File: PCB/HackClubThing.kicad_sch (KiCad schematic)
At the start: 13 parts, among them SW1 SW_Push, SW2 SW_Push, SW3 SW_Push, SW4 SW_Push, SW5 SW_Push, SW6 RotaryEncoder_Switch, U1 MOUDLE-SEEEDUINO-XIAO, U2 ER_OLEDM0.91_1x-I2C

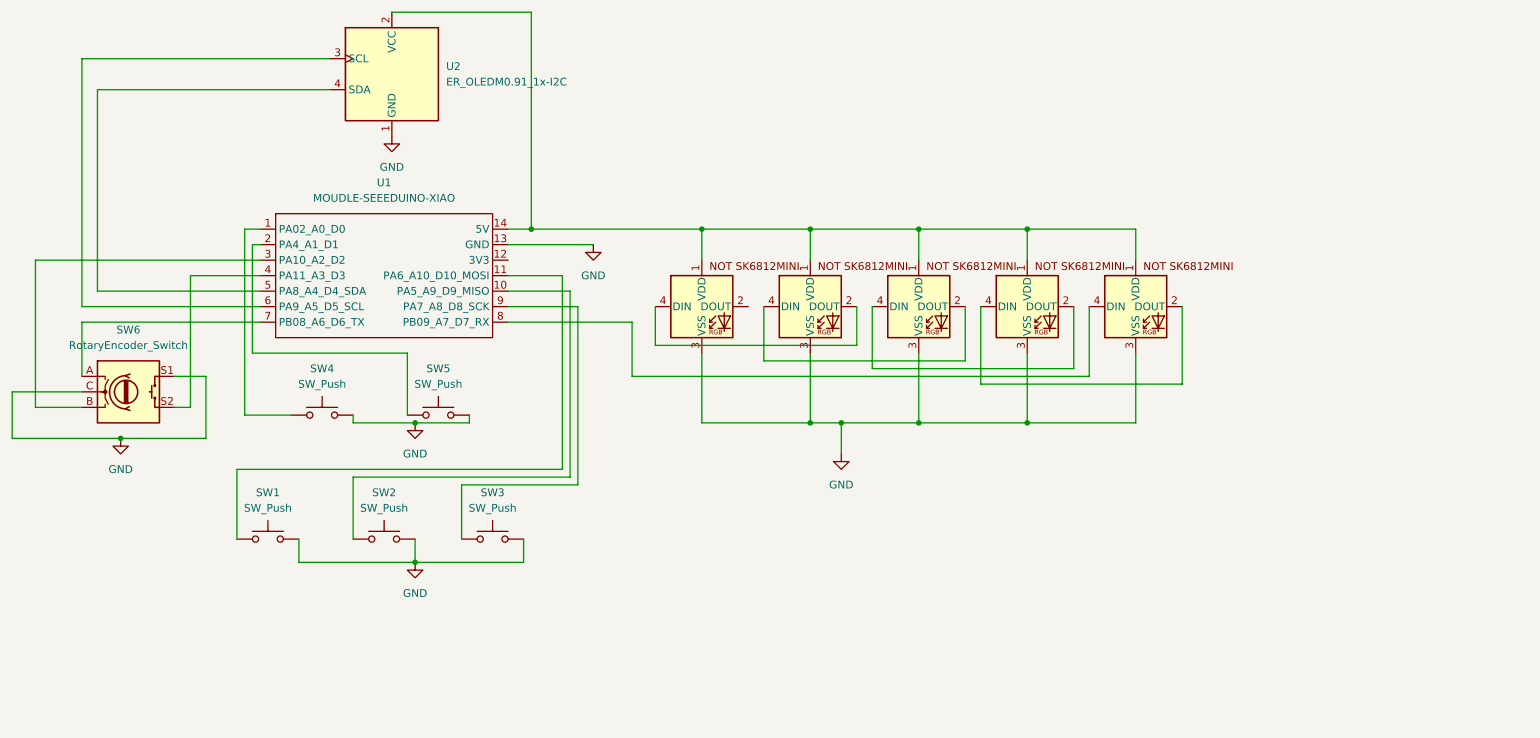
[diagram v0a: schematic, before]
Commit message: Moved Key and LED Locations and added backlighting
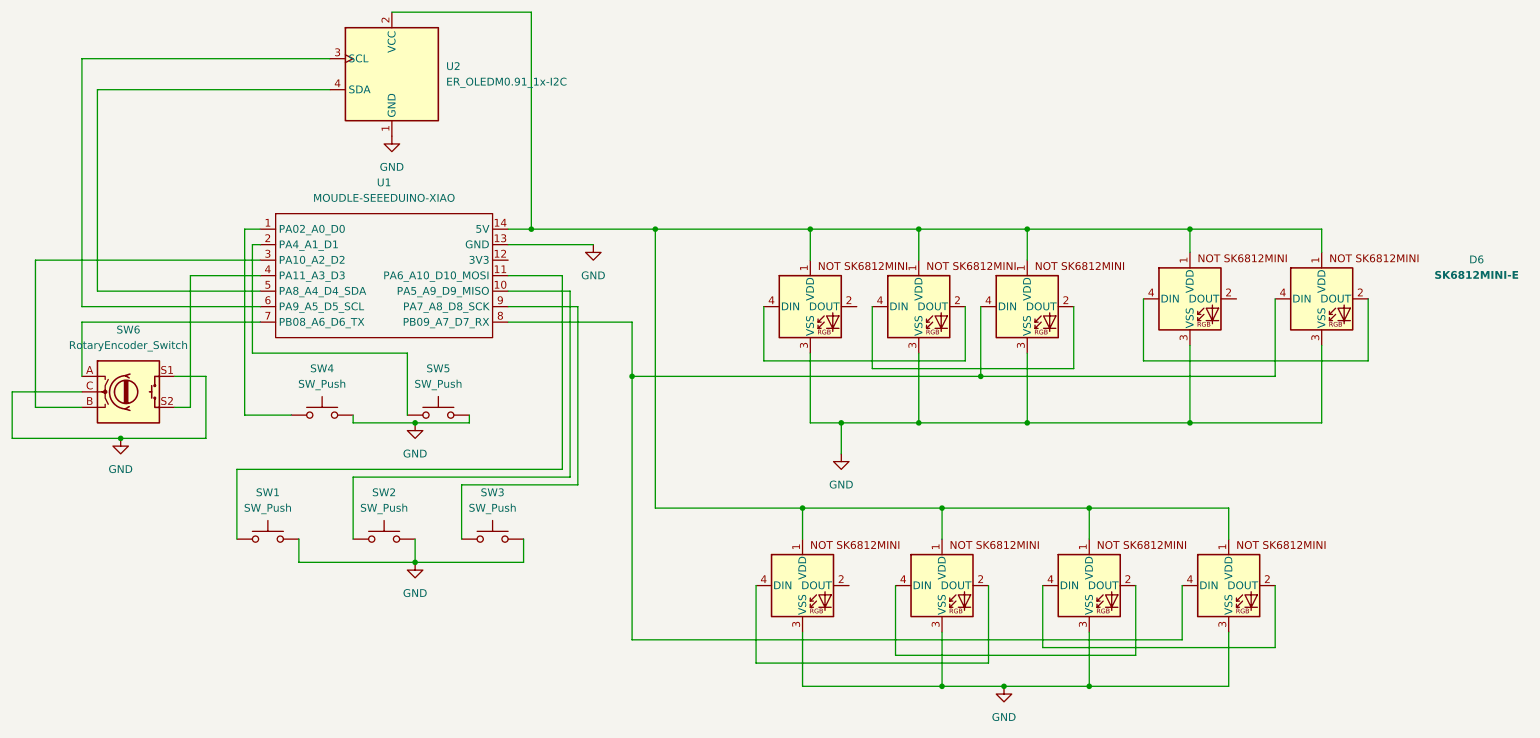
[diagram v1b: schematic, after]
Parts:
- added D6, D7, D8, D9: SK6812MINI-E, HackClubCarePackage:SK6812MINI-E_fixed, symbol HackClubCarePackage:SK6812MINI-E
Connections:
- net GND: now also D6.3 (VSS), D7.3 (VSS), D8.3 (VSS), D9.3 (VSS)
- net at D1.1 (VDD), D2.1 (VDD), D3.1 (VDD)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: now also D6.1 (VDD), D7.1 (VDD), D8.1 (VDD), D9.1 (VDD)
- net at D5.2 (DOUT): no longer D4.4 (DIN)
- net at D5.4 (DIN): now also D6.2 (DOUT); no longer U1.8 (PB09_A7_D7_RX)
- net at D1.4 (DIN): now also D7.2 (DOUT); no longer D2.2 (DOUT)
- new net: D4.4 (DIN), D6.4 (DIN), D9.4 (DIN), U1.8 (PB09_A7_D7_RX)
- new net: D7.4 (DIN), D8.2 (DOUT)
- new net: D8.4 (DIN), D9.2 (DOUT)
